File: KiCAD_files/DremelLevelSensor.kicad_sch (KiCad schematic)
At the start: 5 parts

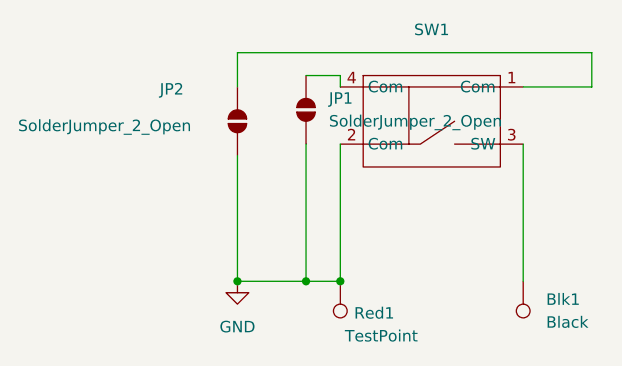
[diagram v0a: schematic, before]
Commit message: Move KiCAD Files folder, add pdf of schematic
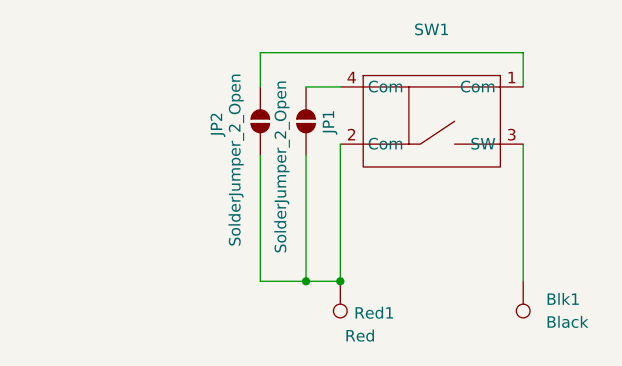
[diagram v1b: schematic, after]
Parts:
- Red1: value TestPoint -> Red
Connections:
- net GND: no longer names the net of JP1.1 (A), JP2.1 (A), Red1.1, SW1.2 (Com)
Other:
- title: (none) -> Dremel Auto Level Board
- moved on the sheet: JP1, JP2
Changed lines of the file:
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@@
 	(generator "eeschema")
 	(generator_version "9.0")
-	(paper "A4")
+	(paper "USLetter")
+	(title_block
+		(title "Dremel Auto Level Board")
+		(date "2026-02-08")
+		(rev "2")
+	)
 	(junction
 		(at 88.9 101.6)
@@
 		(color 0 0 0 0)
 	)
-	(junction
-		(at 81.28 101.6)
-		(diameter 0)
-		(color 0 0 0 0)
-	)
-	(wire
-		(pts
-			(xy 120.65 80.01) (xy 120.65 76.2)
-		)
-		(stroke
-			(width 0)
-			(type default)
-		)
-	)
-	(wire
-		(pts
-			(xy 120.65 80.01) (xy 113.03 80.01)
+	(wire
+		(pts
+			(xy 113.03 80.01) (xy 113.03 76.2)
+		)
+		(stroke
+			(width 0)
+			(type default)
+		)
+	)
+	(wire
+		(pts
+			(xy 83.82 76.2) (xy 113.03 76.2)
+		)
+		(stroke
+			(width 0)
+			(type default)
+		)
+	)
+	(wire
+		(pts
+			(xy 88.9 80.01) (xy 92.71 80.01)
 		)
 		(stroke
@@
 	(wire
 		(pts
-			(xy 81.28 76.2) (xy 81.28 80.01)
-		)
-		(stroke
-			(width 0)
-			(type default)
-		)
-	)
-	(wire
-		(pts
-			(xy 88.9 86.36) (xy 88.9 101.6)
+			(xy 83.82 76.2) (xy 83.82 80.01)
 		)
 		(stroke
@@
 	(wire
 		(pts
-			(xy 92.71 80.01) (xy 92.71 78.74)
-		)
-		(stroke
-			(width 0)
-			(type default)
-		)
-	)
-	(wire
-		(pts
-			(xy 92.71 101.6) (xy 88.9 101.6)
-		)
-		(stroke
-			(width 0)
-			(type default)
-		)
-	)
-	(wire
-		(pts
-			(xy 92.71 78.74) (xy 88.9 78.74)
-		)
-		(stroke
-			(width 0)
-			(type default)
-		)
-	)
-	(wire
-		(pts
-			(xy 81.28 76.2) (xy 120.65 76.2)
-		)
-		(stroke
-			(width 0)
-			(type default)
-		)
-	)
-	(wire
-		(pts
-			(xy 81.28 101.6) (xy 88.9 101.6)
-		)
-		(stroke
-			(width 0)
-			(type default)
-		)
-	)
-	(wire
-		(pts
-			(xy 81.28 87.63) (xy 81.28 101.6)
+			(xy 83.82 101.6) (xy 88.9 101.6)
+		)
+		(stroke
+			(width 0)
+			(type default)
+		)
+	)
+	(wire
+		(pts
+			(xy 88.9 101.6) (xy 92.71 101.6)
+		)
+		(stroke
+			(width 0)
+			(type default)
+		)
+	)
+	(wire
+		(pts
+			(xy 88.9 87.63) (xy 88.9 101.6)
+		)
+		(stroke
+			(width 0)
+			(type default)
+		)
+	)
+	(wire
+		(pts
+			(xy 83.82 87.63) (xy 83.82 101.6)
 		)
 		(stroke
@@
 	(symbol
 		(lib_id "Jumper:SolderJumper_2_Open")
-		(at 81.28 83.82 90)
+		(at 83.82 83.82 90)
 		(unit 1)
 		(exclude_from_sim no)
@@
 		(dnp no)
 		(property "Reference" "JP2"
-			(at 72.644 80.264 90)
+			(at 78.994 82.804 0)
 			(effects
 				(font
@@
 		)
 		(property "Value" "SolderJumper_2_Open"
-			(at 56.896 84.328 90)
+			(at 81.026 78.486 0)
 			(effects
 				(font
@@
 		)
 		(property "Footprint" "Jumper:SolderJumper-2_P1.3mm_Open_RoundedPad1.0x1.5mm"
-			(at 81.28 83.82 0)
+			(at 83.82 83.82 0)
 			(effects
 				(font
@@
 		)
 		(property "Datasheet" "~"
-			(at 81.28 83.82 0)
+			(at 83.82 83.82 0)
 			(effects
 				(font
@@
 		)
 		(property "Description" "Solder Jumper, 2-pole, open"
-			(at 81.28 83.82 0)
+			(at 83.82 83.82 0)
 			(effects
 				(font
@@
 	(symbol
 		(lib_id "Jumper:SolderJumper_2_Open")
-		(at 88.9 82.55 90)
+		(at 88.9 83.82 90)
 		(unit 1)
 		(exclude_from_sim no)
@@
 		(on_board yes)
 		(dnp no)
-		(fields_autoplaced yes)
 		(property "Reference" "JP1"
-			(at 91.44 81.2799 90)
+			(at 91.44 82.5499 0)
 			(effects
 				(font
@@
 		)
 		(property "Value" "SolderJumper_2_Open"
-			(at 91.44 83.8199 90)
+			(at 86.106 79.248 0)
 			(effects
 				(font
@@
 		)
 		(property "Footprint" "Jumper:SolderJumper-2_P1.3mm_Open_RoundedPad1.0x1.5mm"
-			(at 88.9 82.55 0)
+			(at 88.9 83.82 0)
 			(effects
 				(font
@@
 		)
 		(property "Datasheet" "~"
-			(at 88.9 82.55 0)
+			(at 88.9 83.82 0)
 			(effects
 				(font
@@
 		)
 		(property "Description" "Solder Jumper, 2-pole, open"
-			(at 88.9 82.55 0)
+			(at 88.9 83.82 0)
 			(effects
 				(font
@@
 			)
 		)
-		(property "Value" "TestPoint"
+		(property "Value" "Red"
 			(at 93.218 107.696 0)
 			(effects
@@
 					(unit 1)
 				)
-			)
-		)
-	)
-	(symbol
-		(lib_id "power:GND")
-		(at 81.28 101.6 0)
-		(unit 1)
-		(exclude_from_sim no)
-		(in_bom yes)
-		(on_board yes)
-		(dnp no)
-		(fields_autoplaced yes)
-		(property "Reference" "#PWR01"
-			(at 81.28 107.95 0)
-			(effects
-				(font
-					(size 1.27 1.27)
-				)
-				(hide yes)
-			)
-		)
-		(property "Value" "GND"
-			(at 81.28 106.68 0)
-			(effects
-				(font
-					(size 1.27 1.27)
-				)
-			)
-		)
-		(property "Footprint" ""
-			(at 81.28 101.6 0)
-			(effects
-				(font
-					(size 1.27 1.27)
-				)
-				(hide yes)
-			)
-		)
-		(property "Datasheet" ""
-			(at 81.28 101.6 0)
-			(effects
-				(font
-					(size 1.27 1.27)
-				)
-				(hide yes)
-			)
-		)
-		(property "Description" "Power symbol creates a global label with name \"GND\" , ground"
-			(at 81.28 101.6 0)
-			(effects
-				(font
-					(size 1.27 1.27)
-				)
-				(hide yes)
-			)
-		)
-		(pin "1"
-		)
-		(instances
-			(project ""
-				(path "/7accf362-abd1-4df7-ad78-69f9d0334dcd"
-					(reference "#PWR01")
-					(unit 1)
-				)
